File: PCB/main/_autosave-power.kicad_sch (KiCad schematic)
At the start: 28 parts, among them M1 CJ2301 S1, U1 LP2951-33DR, U2 LM324

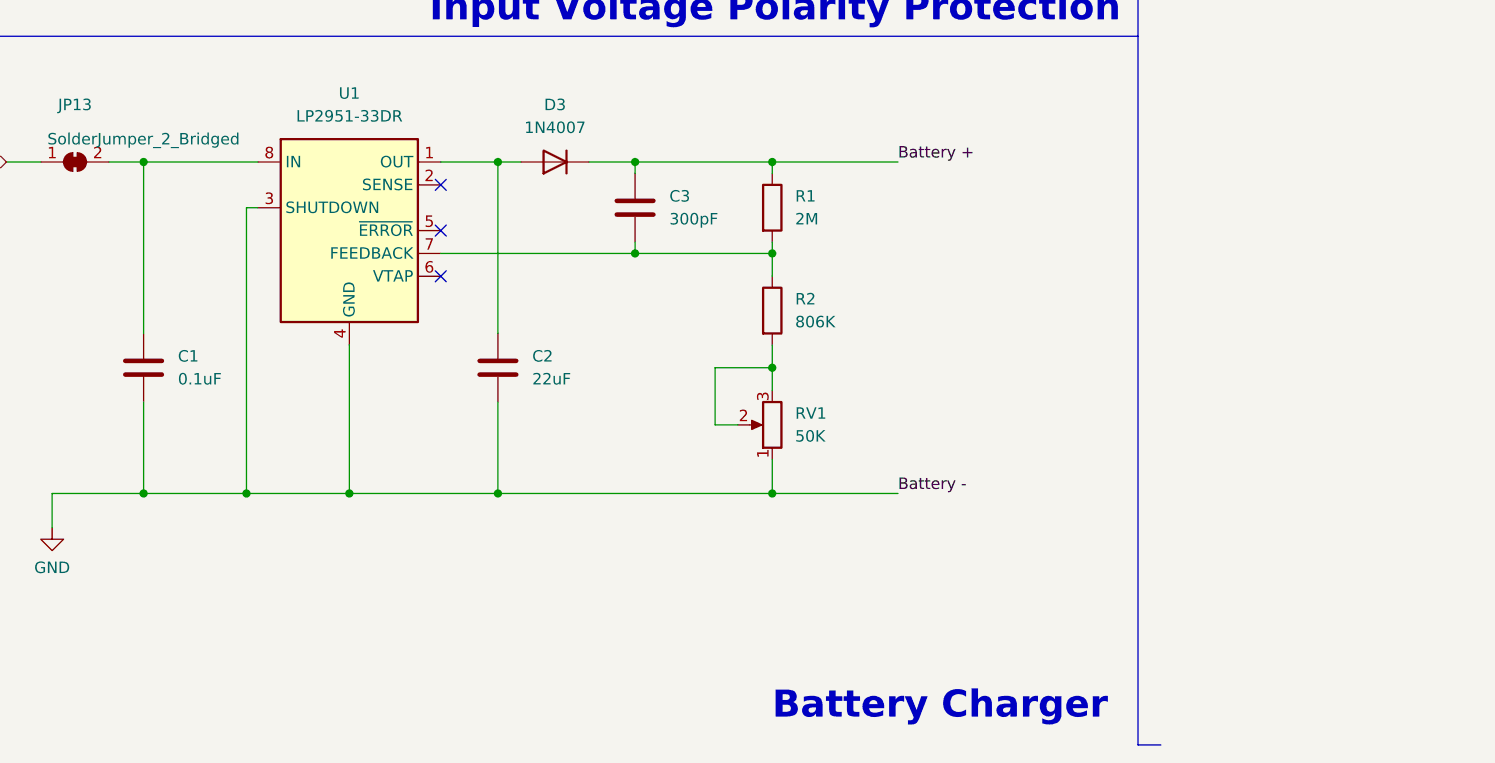
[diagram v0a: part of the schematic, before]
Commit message: Add power flags
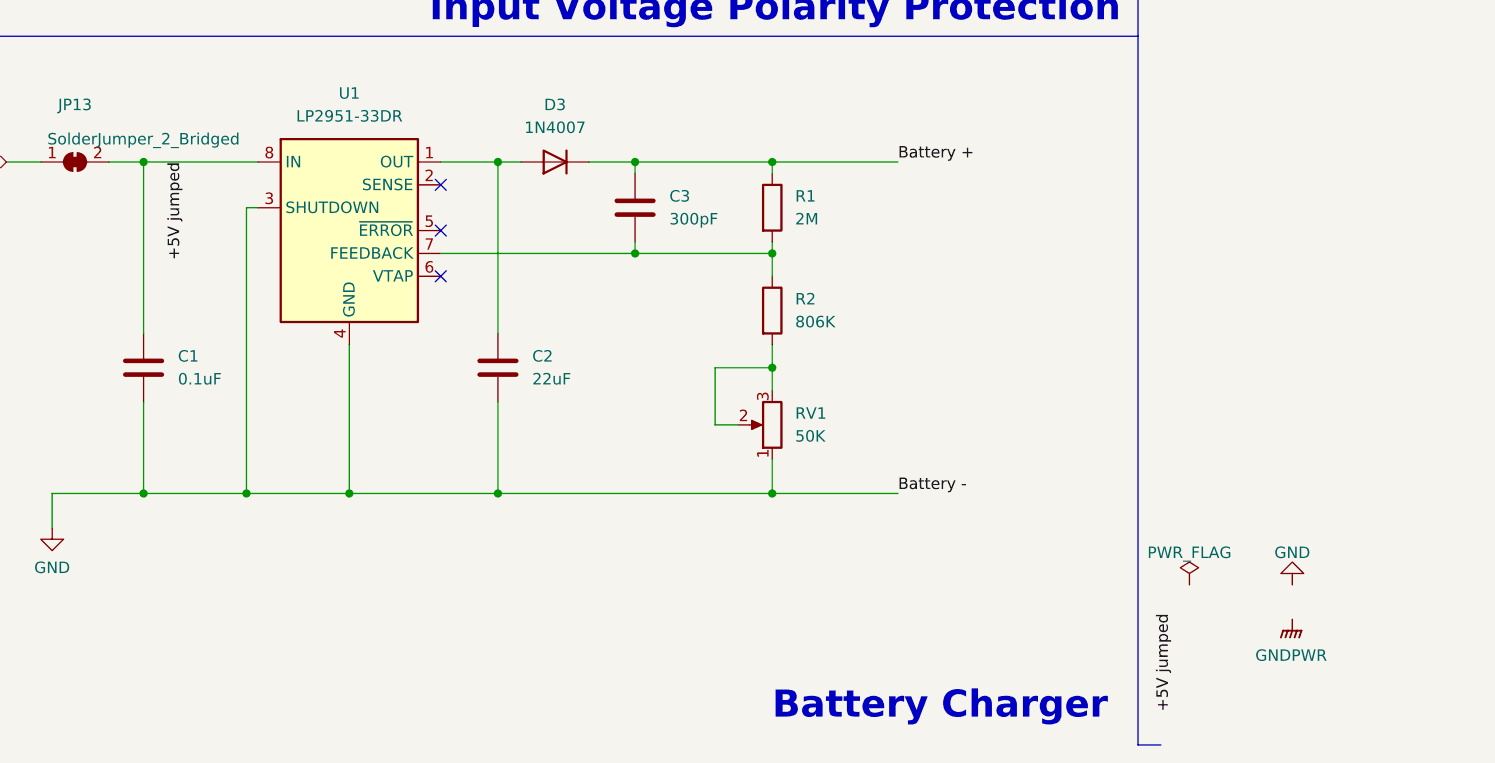
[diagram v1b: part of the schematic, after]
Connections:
- net +5V jumped: now reaches C1.1, JP13.2 (B), U1.8 (IN)
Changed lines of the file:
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@@
     (effects (font (size 1.27 1.27)) (justify left bottom))
+  )
+  (label "+5V jumped" (at 152.4 183.515 270)
+    (effects (font (size 1.27 1.27)) (justify right bottom))
   )
   (label "Battery +" (at 86.36 34.29 0)
@@
   (label "+5V (INPUT PROTECTED)" (at 85.09 99.06 0)
     (effects (font (size 1.27 1.27)) (justify left bottom))
+  )
+  (label "+5V jumped" (at 42.545 133.35 270)
+    (effects (font (size 1.27 1.27)) (justify right bottom))
   )
   (label "+5V (REVERSE PROTECTED)" (at 78.74 66.04 0)
@@
     )
     (property "Datasheet" "" (id 3) (at 246.38 31.75 0)
+      (effects (font (size 1.27 1.27)) hide)
+    )
+    (pin "1")
+  )
+  (symbol (lib_id "power:GNDPWR") (at 165.735 184.15 0) (unit 1)
+    (in_bom yes) (on_board yes) (fields_autoplaced)
+    (property "Reference" "#PWR?" (id 0) (at 165.735 189.23 0)
+      (effects (font (size 1.27 1.27)) hide)
+    )
+    (property "Value" "GNDPWR" (id 1) (at 165.608 188.187 0))
+    (property "Footprint" "" (id 2) (at 165.735 185.42 0)
+      (effects (font (size 1.27 1.27)) hide)
+    )
+    (property "Datasheet" "" (id 3) (at 165.735 185.42 0)
       (effects (font (size 1.27 1.27)) hide)
     )
@@
     (pin "1")
   )
+  (symbol (lib_id "power:PWR_FLAG") (at 154.305 180.34 0) (unit 1)
+    (in_bom yes) (on_board yes) (fields_autoplaced)
+    (property "Reference" "#FLG?" (id 0) (at 154.305 178.435 0)
+      (effects (font (size 1.27 1.27)) hide)
+    )
+    (property "Value" "PWR_FLAG" (id 1) (at 154.305 176.7642 0))
+    (property "Footprint" "" (id 2) (at 154.305 180.34 0)
+      (effects (font (size 1.27 1.27)) hide)
+    )
+    (property "Datasheet" "~" (id 3) (at 154.305 180.34 0)
+      (effects (font (size 1.27 1.27)) hide)
+    )
+    (pin "1")
+  )
   (symbol (lib_id "pspice:MPMOS") (at 256.54 45.72 0) (unit 1)
     (in_bom yes) (on_board yes) (fields_autoplaced)
@@
     (pin "2")
   )
+  (symbol (lib_id "power:GND") (at 165.735 180.34 180) (unit 1)
+    (in_bom yes) (on_board yes) (fields_autoplaced)
+    (property "Reference" "#PWR?" (id 0) (at 165.735 173.99 0)
+      (effects (font (size 1.27 1.27)) hide)
+    )
+    (property "Value" "GND" (id 1) (at 165.735 176.7642 0))
+    (property "Footprint" "" (id 2) (at 165.735 180.34 0)
+      (effects (font (size 1.27 1.27)) hide)
+    )
+    (property "Datasheet" "" (id 3) (at 165.735 180.34 0)
+      (effects (font (size 1.27 1.27)) hide)
+    )
+    (pin "1")
+  )
   (sheet_instances
